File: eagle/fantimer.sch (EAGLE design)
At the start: 17 parts, among them IC1 PIC10F220, K1 PB2032-ND, Q1 2N7000-G, U1 IRM-01-5, X1 732-10957-ND

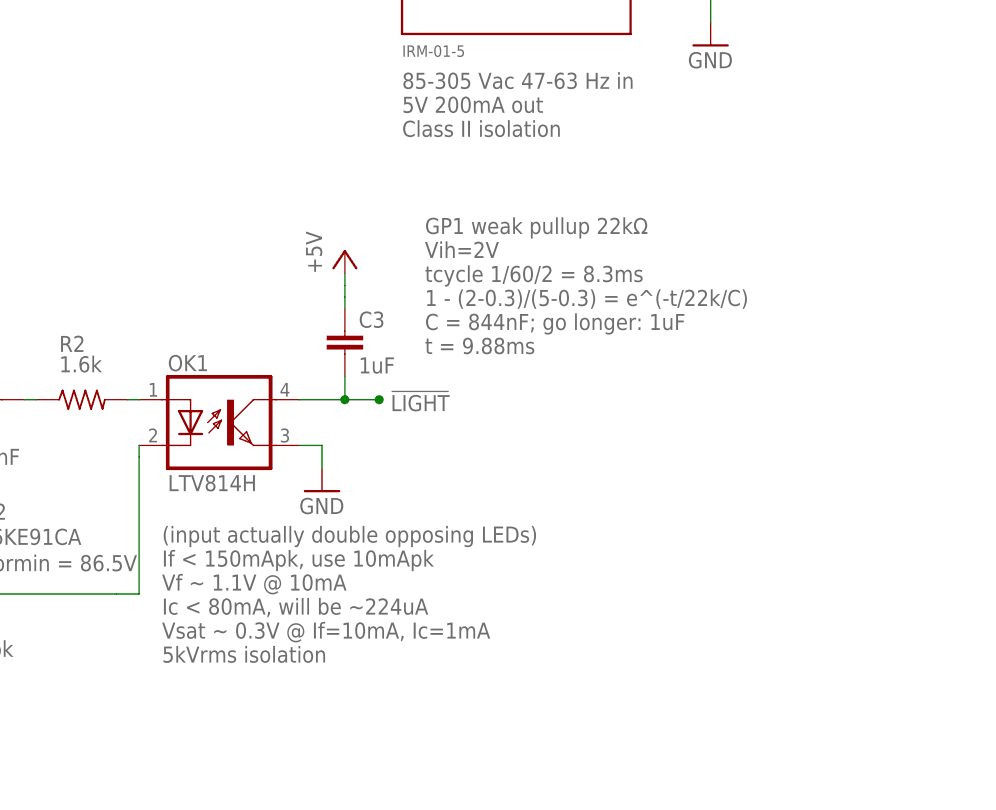
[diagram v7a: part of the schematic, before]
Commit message: Adjust detection cap based on experiment
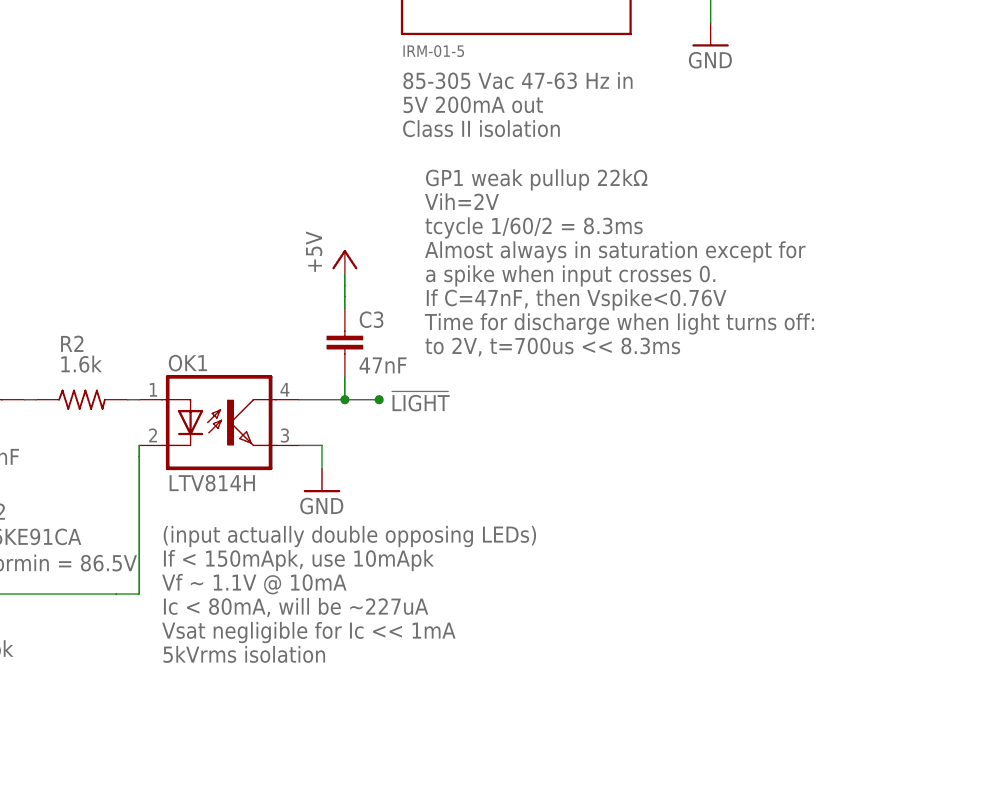
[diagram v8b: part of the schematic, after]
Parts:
- C3: value 1uF -> 47nF
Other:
- note added: "(input actually double opposing LEDs) If < 150mApk, use 10mApk Vf ~ 1.1V @ 10mA Ic < 80mA, will be ~227uA Vsat negligible for Ic << 1mA 5kVrms isolation"
- note added: "GP1 weak pullup 22kΩ Vih=2V tcycle 1/60/2 = 8.3ms Almost always in saturation except for a spike when input crosses 0. If C=47nF, then Vspike<0.76V Time for discharge when light turns off: to 2V, t=700us << 8.3ms"
- note removed: "(input actually double opposing LEDs) If < 150mApk, use 10mApk Vf ~ 1.1V @ 10mA Ic < 80mA, will be ~224uA Vsat ~ 0.3V @ If=10mA, Ic=1mA 5kVrms isolation"
- note removed: "GP1 weak pullup 22kΩ Vih=2V tcycle 1/60/2 = 8.3ms 1 - (2-0.3)/(5-0.3) = e^(-t/22k/C) C = 844nF; go longer: 1uF t = 9.88ms"
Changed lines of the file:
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@@
 <part name="P+6" library="supply1" library_urn="urn:adsk.eagle:library:371" deviceset="+5V" device=""/>
 <part name="GND5" library="supply1" library_urn="urn:adsk.eagle:library:371" deviceset="GND" device=""/>
-<part name="C3" library="rcl" library_urn="urn:adsk.eagle:library:334" deviceset="C-EU" device="025-025X050" package3d_urn="urn:adsk.eagle:package:23629/2" value="1uF"/>
+<part name="C3" library="rcl" library_urn="urn:adsk.eagle:library:334" deviceset="C-EU" device="025-025X050" package3d_urn="urn:adsk.eagle:package:23629/2" value="47nF"/>
 <part name="P+2" library="supply1" library_urn="urn:adsk.eagle:library:371" deviceset="+5V" device=""/>
 <part name="IC1" library="microchip-addl" deviceset="PIC10F220" device="-I/P" package3d_urn="urn:adsk.eagle:package:14440/1" value="PIC10F220"/>
@@
 If &lt; 150mApk, use 10mApk
 Vf ~ 1.1V @ 10mA
-Ic &lt; 80mA, will be ~224uA
-Vsat ~ 0.3V @ If=10mA, Ic=1mA
+Ic &lt; 80mA, will be ~227uA
+Vsat negligible for Ic &lt;&lt; 1mA
 5kVrms isolation</text>
 <text x="7.62" y="107.95" size="1.778" layer="96" rot="MR180">Vin = 120Vrms = 169.7Vpk
@@
 Vih=2V
 tcycle 1/60/2 = 8.3ms
-1 - (2-0.3)/(5-0.3) = e^(-t/22k/C)
-C = 844nF; go longer: 1uF
-t = 9.88ms</text>
+Almost always in saturation except for
+a spike when input crosses 0.
+If C=47nF, then Vspike&lt;0.76V
+Time for discharge when light turns off:
+to 2V, t=700us &lt;&lt; 8.3ms</text>
 <text x="17.78" y="134.62" size="1.778" layer="97">CF14JT1K60‎ - 250mW</text>
 <text x="11.43" y="121.92" size="1.778" layer="97">334MMR250K‎ - 250V</text>
